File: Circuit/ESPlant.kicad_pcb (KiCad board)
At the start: 2 copper layers, 97 x 77.5 mm, 72 parts, among them P1 SOIL, P101 CONN_DIGITAL, P102 CONN_ANALOG, P103 CONN_SERIAL, P104 CONN_I2C, P105 SOLAR, P106 USB_5PIN_SHELL, P109 CONN_PWR, P110 CONN_01X05, P111 UV, P112 TEMP, P113 NEOPIXEL, P114 PIR, Q101 FDN340P, Q201 FDN340P, Q202 FDN340P, Q203 FDN340P, SW101 RESET, SW102 PRGM, SW103 RESET, SW104 SS12D00, U101 STM32F042F, U103 ESP-12E, U201 CN3063, U202 MCP6002, U301 BME280, U302 ADXL345

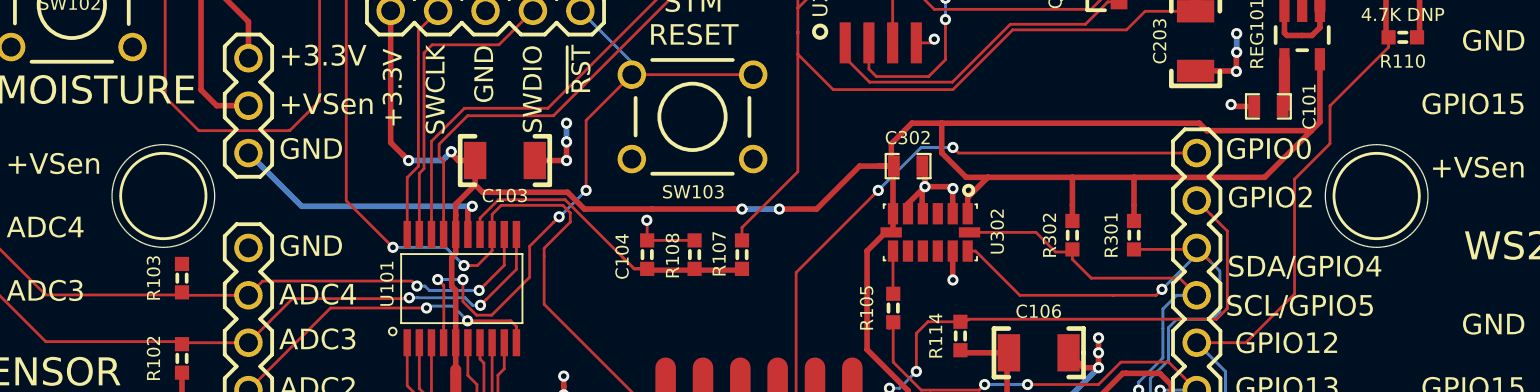
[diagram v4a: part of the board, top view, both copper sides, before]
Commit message: Add LCA Geelong wave logo to back of V1.1 PCB
Thanks to @rdpowers for the idea and @dtbell91 for providing a logo at
short notice.
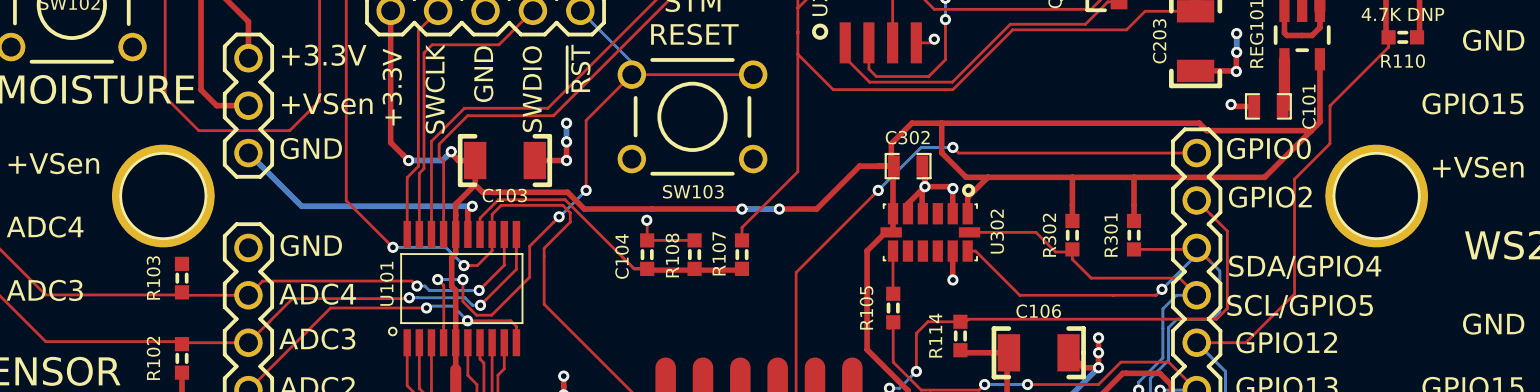
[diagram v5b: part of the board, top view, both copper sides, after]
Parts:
- added G***: LOGO, Plant:lca2016_logo, B.Cu at (186.8, 82.5)

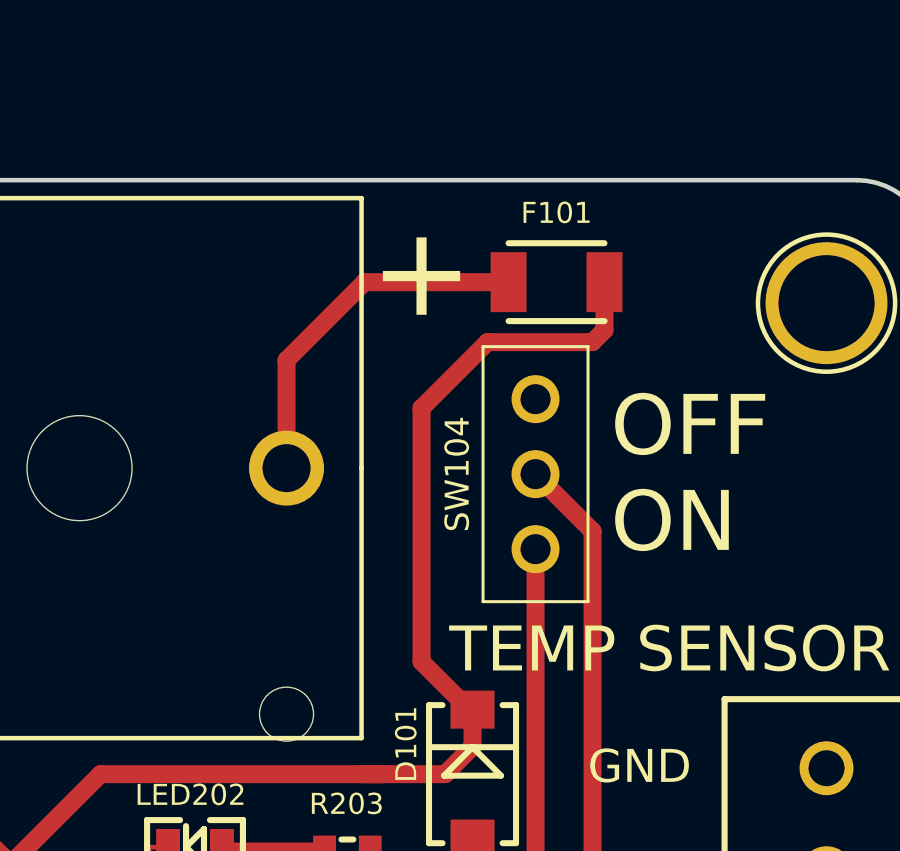
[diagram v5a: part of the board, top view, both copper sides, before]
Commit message: Tweak fuse a little further away from power switch body (being paranoid)
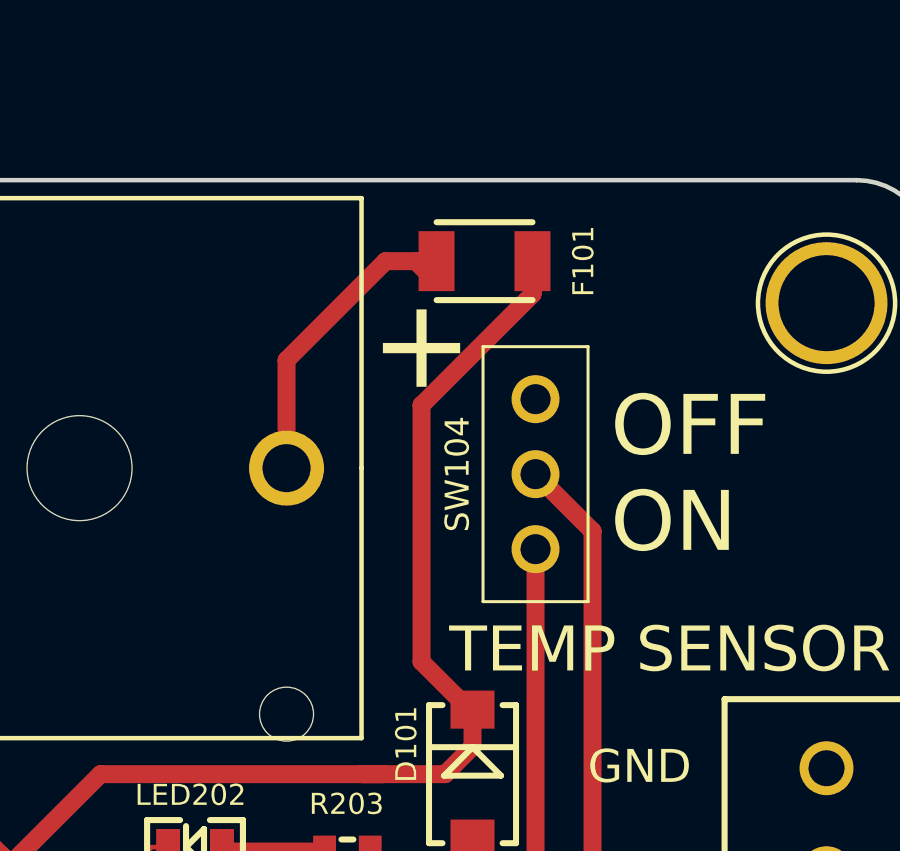
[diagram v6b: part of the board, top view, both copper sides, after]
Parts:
- moved F101 2.50 mm to (224.1, 63.2)
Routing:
- net /Power/VBAT: track 69.7 -> 67.7 mm
- net /BAT+: track 12.1 -> 11.0 mm
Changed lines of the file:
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@@
 (kicad_pcb (version 4) (host pcbnew 0.201511110417+6307~30~ubuntu15.10.1-product)
   (general
-    (links 0)
+    (links 184)
     (no_connects 0)
-    (area 141.924999 60.424999 239.075001 138.075001)
+    (area 126.97 50.8 241.300001 138.419)
     (thickness 1.6)
     (drawings 127)
-    (tracks 1087)
+    (tracks 1088)
     (zones 0)
     (modules 73)
@@
   (page A4)
   (layers
-    (0 F.Cu signal hide)
+    (0 F.Cu signal)
     (31 B.Cu signal)
     (32 B.Adhes user)
@@
     (34 B.Paste user)
     (35 F.Paste user hide)
-    (36 B.SilkS user)
-    (37 F.SilkS user hide)
+    (36 B.SilkS user hide)
+    (37 F.SilkS user)
     (38 B.Mask user)
     (39 F.Mask user)
@@
   )
   (setup
-    (last_trace_width 0.15)
+    (last_trace_width 0.6)
     (user_trace_width 0.15)
     (user_trace_width 0.2)
@@
   )
   (module FT:1210 (layer F.Cu)
-    (at 226.5 63.9)
-    (fp_text reference F101 (at -0.00234 -2.3 180) (layer F.SilkS)
+    (at 224.1 63.2)
+    (fp_text reference F101 (at 3.3 0 270) (layer F.SilkS)
       (effects (font (size 0.7 0.7) (thickness 0.15)))
     )
@@
       (effects (font (size 1 1) (thickness 0.15)))
     )
-    (fp_text user + (at -23.5 6.5 180) (layer F.SilkS)
+    (fp_text user + (at -23.5 4.1 180) (layer F.SilkS)
       (effects (font (size 3 3) (thickness 0.45)))
     )
@@
     (effects (font (size 1.1 1.1) (thickness 0.2)) (justify left))
   )
-  (segment (start 217.5 66.5) (end 217.5 70.1) (width 0.6) (layer F.Cu) (net 1))
-  (segment (start 224.90234 63.9) (end 220.1 63.9) (width 0.6) (layer F.Cu) (net 1))
-  (segment (start 220.1 63.9) (end 217.5 66.5) (width 0.6) (layer F.Cu) (net 1))
+  (segment (start 222.50234 63.2) (end 221.80234 63.2) (width 0.6) (layer F.Cu) (net 1))
+  (segment (start 217.5 70.1) (end 217.5 66.5) (width 0.6) (layer F.Cu) (net 1))
+  (segment (start 217.5 66.5) (end 220.8 63.2) (width 0.6) (layer F.Cu) (net 1))
+  (segment (start 220.8 63.2) (end 221.80234 63.2) (width 0.6) (layer F.Cu) (net 1))
+  (segment (start 221.80234 63.2) (end 222.50234 63.9) (width 0.6) (layer F.Cu) (net 1))
   (via (at 222 85.3) (size 0.6) (drill 0.3) (layers F.Cu B.Cu) (net 2))
   (segment (start 222 84.2) (end 222 85.3) (width 0.6) (layer F.Cu) (net 2))
@@
   (segment (start 189 106.14168) (end 189 105.5929) (width 0.15) (layer F.Cu) (net 7))
   (segment (start 189 106.14168) (end 189.20066 106.14168) (width 0.15) (layer F.Cu) (net 7))
-  (segment (start 227.69715 65.9) (end 224.19771 65.9) (width 0.6) (layer F.Cu) (net 8))
-  (segment (start 224.19771 65.9) (end 222 68.09771) (width 0.6) (layer F.Cu) (net 8))
-  (segment (start 228.09766 63.9) (end 228.09766 65.49949) (width 0.6) (layer F.Cu) (net 8))
-  (segment (start 228.09766 65.49949) (end 227.69715 65.9) (width 0.6) (layer F.Cu) (net 8))
-  (segment (start 222 68.09771) (end 222 76.55149) (width 0.6) (layer F.Cu) (net 8))
+  (segment (start 225.69766 63.2) (end 225.69766 64.30005) (width 0.6) (layer F.Cu) (net 8))
+  (segment (start 225.69766 63.9) (end 225.69766 64.30005) (width 0.6) (layer F.Cu) (net 8))
+  (segment (start 225.69766 64.30005) (end 222 67.99771) (width 0.6) (layer F.Cu) (net 8))
+  (segment (start 222 67.99771) (end 222 76.55149) (width 0.6) (layer F.Cu) (net 8))
   (segment (start 222 76.55149) (end 223.59967 78.15116) (width 0.6) (layer F.Cu) (net 8))
   (segment (start 223.59967 78.15116) (end 223.7 78.15116) (width 0.6) (layer F.Cu) (net 8))

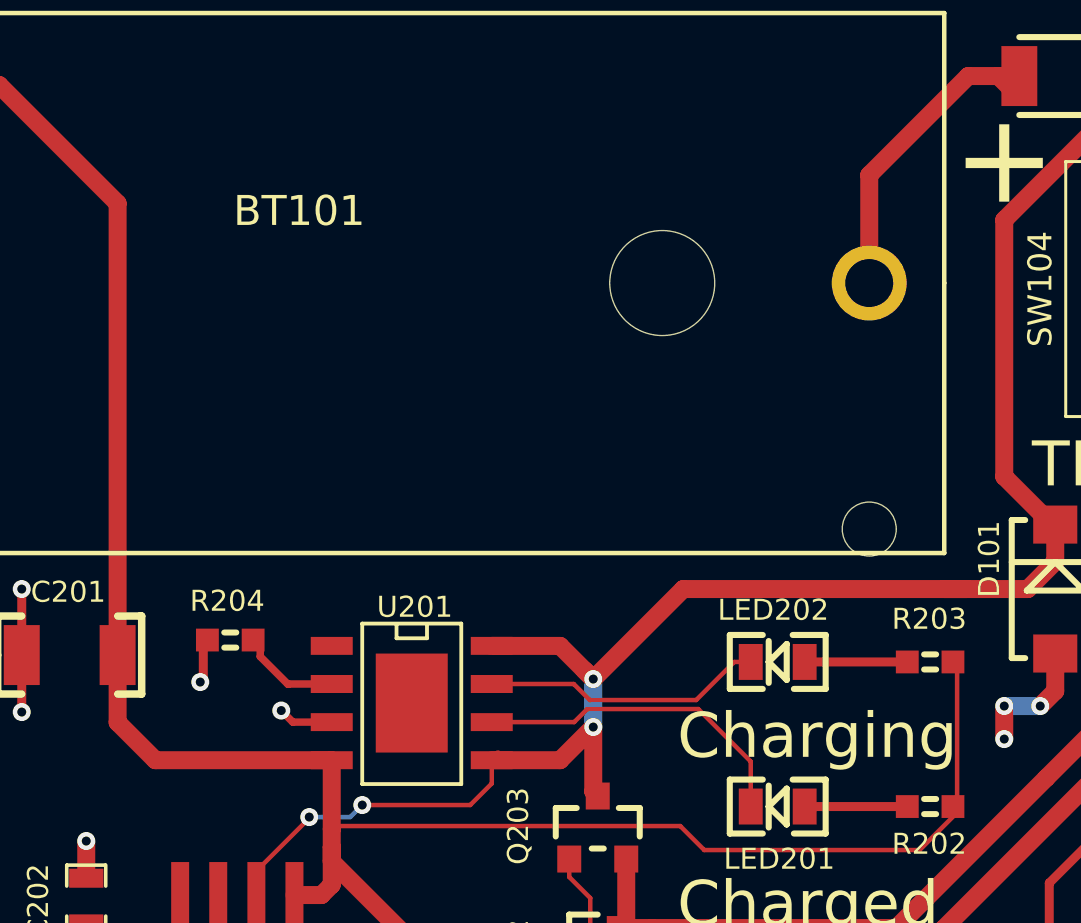
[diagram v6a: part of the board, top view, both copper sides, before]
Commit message: Add NTC thermistor for overtemperature charging cutoff
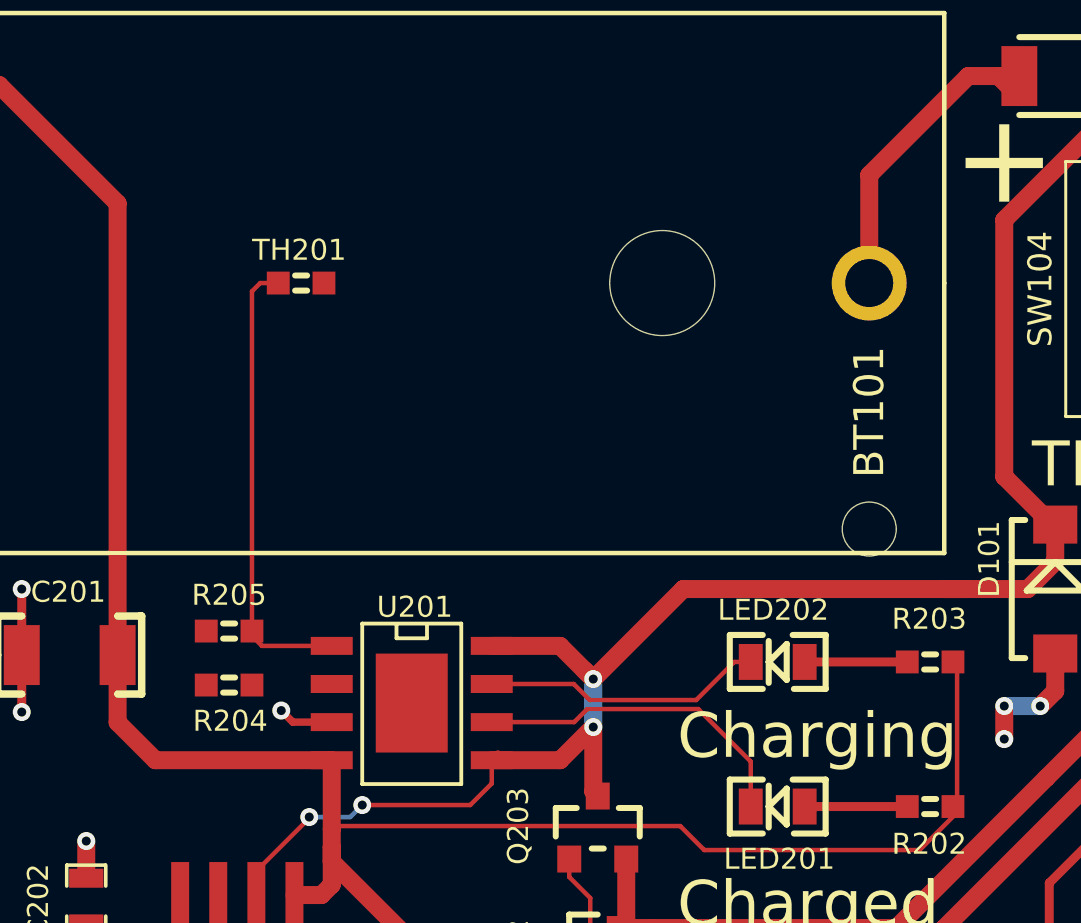
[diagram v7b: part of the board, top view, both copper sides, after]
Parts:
- added R205: 7.15K 1%, FT:0603, F.Cu at (196.2, 81.7)
- added TH201: 10K NTC, FT:0603, F.Cu at (198.6, 70.1)
- R204: value 8.2K -> 7.15K 1%
- moved R204 1.50 mm to (196.2, 83.5)
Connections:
- U201 pad 1: GND -> Net-(R205-Pad2)
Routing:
- net Net-(R205-Pad2): track 0.00 -> 15.3 mm
- net Net-(R204-Pad1): track 3.17 -> 0.00 mm
- net GND: track 152.6 -> 151.1 mm, vias 63 -> 62
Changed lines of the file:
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@@
 (kicad_pcb (version 4) (host pcbnew 0.201511110417+6307~30~ubuntu15.10.1-product)
   (general
-    (links 184)
-    (no_connects 0)
-    (area 126.97 50.8 241.300001 138.419)
+    (links 187)
+    (no_connects 4)
+    (area 141.924999 60.424999 239.075001 138.075001)
     (thickness 1.6)
     (drawings 127)
-    (tracks 1088)
+    (tracks 1086)
     (zones 0)
-    (modules 73)
-    (nets 46)
+    (modules 75)
+    (nets 47)
   )
   (page A4)
@@
   )
   (setup
-    (last_trace_width 0.6)
+    (last_trace_width 0.15)
     (user_trace_width 0.15)
     (user_trace_width 0.2)
@@
   (net 44 /GPIO0_BOOT)
   (net 45 /VSWITCHED)
+  (net 46 "Net-(R205-Pad2)")
   (net_class Default "This is the default net class."
     (clearance 0.15)
@@
     (add_net "Net-(Q101-PadG)")
     (add_net "Net-(R204-Pad1)")
+    (add_net "Net-(R205-Pad2)")
   )
   (net_class Power ""
@@
       (net 8 /Power/VBAT))
     (pad 1 smd rect (at -1.905 2.667 270) (size 0.59944 1.39954) (layers F.Cu F.Paste F.Mask)
-      (net 2 GND))
+      (net 46 "Net-(R205-Pad2)"))
     (pad 7 smd rect (at -0.635 -2.667 270) (size 0.59944 1.39954) (layers F.Cu F.Paste F.Mask)
       (net 13 /Power/~CHRG))
@@
   (module Plant:CR123_Holder (layer F.Cu)
     (at 198.5 70.1 180)
-    (fp_text reference BT101 (at 0 2.4 180) (layer F.SilkS)
+    (fp_text reference BT101 (at -19 -4.3 270) (layer F.SilkS)
       (effects (font (size 1 1) (thickness 0.15)))
     )
@@
   )
   (module FT:0603 (layer F.Cu)
-    (at 196.20084 82 180)
+    (at 196.162 83.5 180)
     (attr smd)
-    (fp_text reference R204 (at 0.10084 1.3 180) (layer F.SilkS)
+    (fp_text reference R204 (at -0.038 -1.2 180) (layer F.SilkS)
       (effects (font (size 0.7 0.7) (thickness 0.15)))
     )
-    (fp_text value 8.2K (at 0.1 0.8 180) (layer F.SilkS) hide
+    (fp_text value "7.15K 1%" (at 0.1 0.8 180) (layer F.SilkS) hide
       (effects (font (size 0.4 0.4) (thickness 0.1)))
     )
@@
       (xy 15.577717 7.155143) (xy 15.87632 7.170224) (xy 16.172951 7.156915)) (layer B.SilkS) (width 0.01))
   )
+  (module FT:0603 (layer F.Cu)
+    (at 196.162 81.7)
+    (attr smd)
+    (fp_text reference R205 (at 0 -1.2) (layer F.SilkS)
+      (effects (font (size 0.7 0.7) (thickness 0.15)))
+    )
+    (fp_text value "7.15K 1%" (at 0.1 0.8) (layer Eco1.User) hide
+      (effects (font (size 0.4 0.4) (thickness 0.1)))
+    )
+    (fp_line (start -0.20066 0.25146) (end 0.20066 0.25146) (layer F.SilkS) (width 0.20066))
+    (fp_line (start -0.20066 -0.25146) (end 0.20066 -0.25146) (layer F.SilkS) (width 0.20066))
+    (pad 1 smd rect (at -0.762 0) (size 0.762 0.762) (layers F.Cu F.Paste F.Mask)
+      (net 6 /Power/VIN))
+    (pad 2 smd rect (at 0.762 0) (size 0.762 0.762) (layers F.Cu F.Paste F.Mask)
+      (net 46 "Net-(R205-Pad2)"))
+    (model smd\resistors\R0603.wrl
+      (at (xyz 0 0 0.001))
+      (scale (xyz 0.5 0.5 0.5))
+      (rotate (xyz 0 0 0))
+    )
+  )
+  (module FT:0603 (layer F.Cu)
+    (at 198.562 70.1)
+    (attr smd)
+    (fp_text reference TH201 (at -0.062 -1.1) (layer F.SilkS)
+      (effects (font (size 0.7 0.7) (thickness 0.15)))
+    )
+    (fp_text value "10K NTC" (at 0.1 0.8) (layer Eco1.User) hide
+      (effects (font (size 0.4 0.4) (thickness 0.1)))
+    )
+    (fp_line (start -0.20066 0.25146) (end 0.20066 0.25146) (layer F.SilkS) (width 0.20066))
+    (fp_line (start -0.20066 -0.25146) (end 0.20066 -0.25146) (layer F.SilkS) (width 0.20066))
+    (pad 1 smd rect (at -0.762 0) (size 0.762 0.762) (layers F.Cu F.Paste F.Mask)
+      (net 46 "Net-(R205-Pad2)"))
+    (pad 2 smd rect (at 0.762 0) (size 0.762 0.762) (layers F.Cu F.Paste F.Mask)
+      (net 2 GND))
+    (model smd\resistors\R0603.wrl
+      (at (xyz 0 0 0.001))
+      (scale (xyz 0.5 0.5 0.5))
+      (rotate (xyz 0 0 0))
+    )
+  )
   (gr_text SCL/GPIO5 (at 224 109.8) (layer B.SilkS)
     (effects (font (size 1.1 1.1) (thickness 0.2)) (justify left mirror))
@@
   (segment (start 177.9 102) (end 179.6 102) (width 0.3) (layer F.Cu) (net 2))
   (via (at 179.6 102) (size 0.6) (drill 0.3) (layers F.Cu B.Cu) (net 2))
-  (segment (start 195.30168 83.298328) (end 195.200008 83.4) (width 0.3) (layer F.Cu) (net 2))
-  (segment (start 195.30168 82) (end 195.30168 83.298328) (width 0.3) (layer F.Cu) (net 2))
-  (via (at 195.200008 83.4) (size 0.6) (drill 0.3) (layers F.Cu B.Cu) (net 2))
   (segment (start 219.00996 92.510728) (end 218.974616 92.475384) (width 0.3) (layer F.Cu) (net 2))
   (segment (start 219.00996 93.98) (end 219.00996 92.510728) (width 0.3) (layer F.Cu) (net 2))
@@
   (segment (start 202.64234 125.5) (end 203.2 126.05766) (width 0.15) (layer F.Cu) (net 41))
   (segment (start 203.2 126.05766) (end 203.2 126.25832) (width 0.15) (layer F.Cu) (net 41))
-  (segment (start 197.2 82.15) (end 197.2 82.55) (width 0.25) (layer F.Cu) (net 42))
-  (segment (start 197.2 82.55) (end 198.12561 83.47561) (width 0.25) (layer F.Cu) (net 42))
-  (segment (start 198.12561 83.47561) (end 198.13622 83.465) (width 0.25) (layer F.Cu) (net 42))
-  (segment (start 198.13622 83.465) (end 199.583 83.465) (width 0.25) (layer F.Cu) (net 42))
   (segment (start 197.9 123.5) (end 202.724 123.5) (width 0.15) (layer F.Cu) (net 43))
   (segment (start 202.724 123.5) (end 203 123.224) (width 0.15) (layer F.Cu) (net 43))
@@
   (segment (start 219.95992 93.98) (end 219.95992 94.87944) (width 0.3) (layer F.Cu) (net 45))
   (segment (start 219.95992 94.87944) (end 219.53936 95.3) (width 0.3) (layer F.Cu) (net 45))
+  (segment (start 196.924 70.376) (end 197.2 70.1) (width 0.15) (layer F.Cu) (net 46))
+  (segment (start 197.2 70.1) (end 197.8 70.1) (width 0.15) (layer F.Cu) (net 46))
+  (segment (start 196.924 81.7) (end 196.924 70.376) (width 0.15) (layer F.Cu) (net 46))
+  (segment (start 199.583 82.195) (end 197.257 82.195) (width 0.15) (layer F.Cu) (net 46))
+  (segment (start 197.257 82.195) (end 196.762 81.7) (width 0.15) (layer F.Cu) (net 46))
   (zone (net 2) (net_name GND) (layer F.Cu) (hatch edge 0.508)
     (connect_pads (clearance 0.4))
